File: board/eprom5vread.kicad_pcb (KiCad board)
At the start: 4 copper layers, 161 x 112 mm, 59 parts, among them J101 DEBUG, J102 UART, J201 Conn_02x21_Counter_Clockwise, J301 Barrel_Jack, SW101 RST, U101 STM32G0B0CETx, U201 TXB0108PW, U202 TXB0108PW, U203 TXB0108PW, U204 TXB0108PW, U205 TXB0108PW, U301 NCP1117ST33T3G, U302 NCP1117ST50T3G

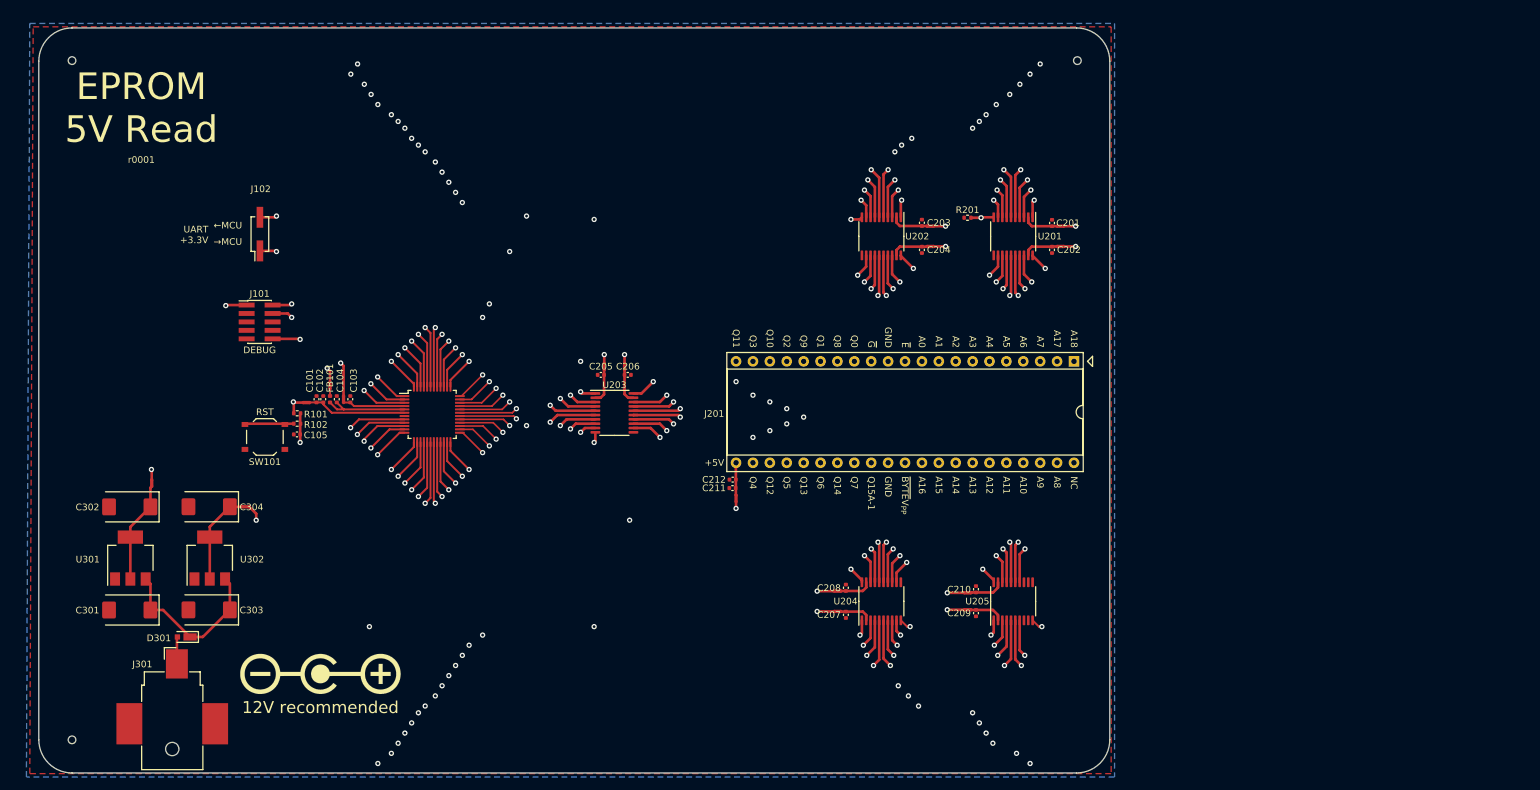
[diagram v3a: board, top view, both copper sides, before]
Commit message: redo board to use I2C port expanders (and smaller MCU)
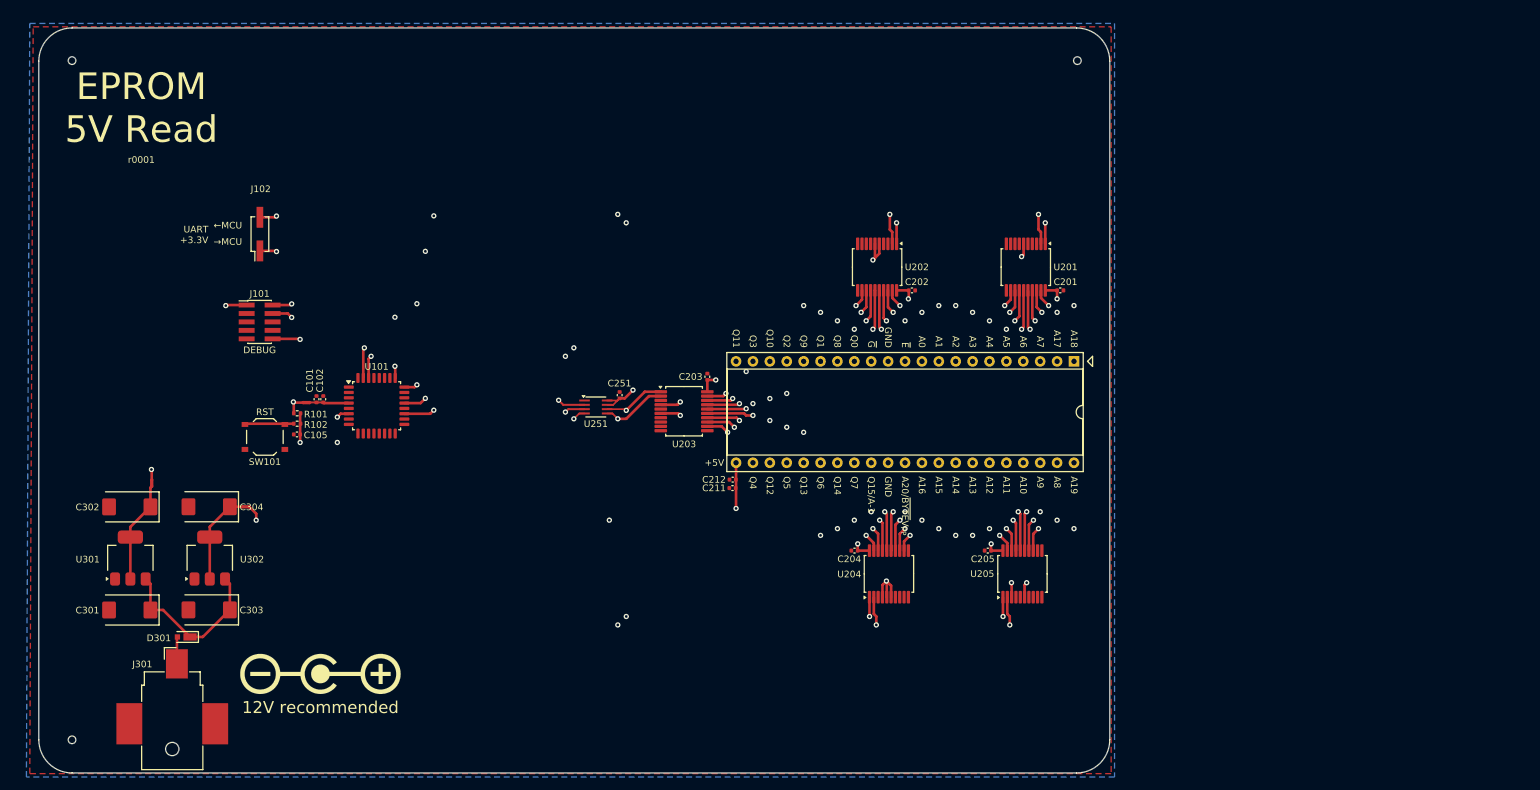
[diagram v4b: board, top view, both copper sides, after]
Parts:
- removed C103: 1µF, Capacitor_SMD:C_0402_1005Metric
- removed C104, C206, C207, C208, C209, C210: 100nF, Capacitor_SMD:C_0402_1005Metric
- removed FB101: 600Ω @ 100MHz, Inductor_SMD:L_0402_1005Metric
- removed NT102, NT103, NT14, NT201, NT202, NT203, NT204, NT205, NT206, NT207, NT208, NT209, NT210: NetTie_2, NetTie:NetTie-2_SMD_Pad0.5mm
- removed R201: 10kΩ, Resistor_SMD:R_0402_1005Metric
- added C251: 100nF, Capacitor_SMD:C_0402_1005Metric, F.Cu at (131.9, 82.3)
- added U251: PCA9306DCTR, Package_SO:SSOP-8_2.95x2.8mm_P0.65mm, F.Cu at (128.3, 84.1)
- U101: footprint Package_QFP:LQFP-48_7x7mm_P0.5mm -> Package_QFP:LQFP-32_7x7mm_P0.8mm
- U201, U202, U203, U204, U205: value TXB0108PW -> MCP23008-E/SS; footprint Package_SO:TSSOP-20_4.4x6.5mm_P0.65mm -> Package_SO:SSOP-20_5.3x7.2mm_P0.65mm
- moved C205 63.9 mm to (187.2, 105.7), turned to 0 degrees
- moved C204 46.3 mm to (167.2, 105.7), turned to 0 degrees
- moved C203 39.7 mm to (145.0, 79.5), turned to -90 degrees
- moved C202 21.9 mm to (175.8, 66.5), turned to 180 degrees
- moved U203 10.5 mm to (141.5, 84.7)
- moved C201 10.2 mm to (198.1, 66.5), turned to 180 degrees
- moved U101 8.45 mm to (95.3, 83.9)
- moved U201 5.00 mm to (192.9, 63.0)
- moved U202 4.67 mm to (170.6, 63.0)
- moved U205 4.35 mm to (192.4, 109.2)
- moved U204 4.27 mm to (172.3, 109.2)
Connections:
- net /EPROM/5V_A0 renamed /EPROM/A0
- net /EPROM/5V_A10 renamed /EPROM/A10
- net /EPROM/5V_A11 renamed /EPROM/A11
- net /EPROM/5V_A12 renamed /EPROM/A12
- net /EPROM/5V_A14 renamed /EPROM/A14
- net /EPROM/5V_A15 renamed /EPROM/A15
- net /EPROM/5V_A16 renamed /EPROM/A16
- net /EPROM/5V_A17 renamed /EPROM/A17
- net /EPROM/5V_A2 renamed /EPROM/A2
- net /EPROM/5V_A3 renamed /EPROM/A3
- net /EPROM/5V_A4 renamed /EPROM/A4
- net /EPROM/5V_A5 renamed /EPROM/A5
- net /EPROM/5V_A6 renamed /EPROM/A6
- net /EPROM/5V_A7 renamed /EPROM/A7
- net /EPROM/5V_A8 renamed /EPROM/A8
- net /EPROM/5V_A9 renamed /EPROM/A9
- net /EPROM/5V_Q0 renamed /EPROM/Q0
- net /EPROM/5V_Q1 renamed /EPROM/Q1
- net /EPROM/5V_Q14 renamed /EPROM/Q14
- net /EPROM/5V_Q15A-1 renamed /EPROM/Q15_A-1
- net /EPROM/5V_Q7 renamed /EPROM/Q7
- net /EPROM/5V_Q8 renamed /EPROM/Q8
- net /EPROM/5V_Q9 renamed /EPROM/Q9
- net /EPROM/5V_~{BYTE}V_{PP} renamed /EPROM/A20_~{BYTE}V_{PP}
- net /EPROM/5V_~{E} renamed /EPROM/~{E}
- net /EPROM/5V_~{G} renamed /EPROM/~{G}
- C201 pad 1: Net-(U201-V_{CCA}) -> /EPROM/GND
- C201 pad 2: /EPROM/GND -> /EPROM/+5V
- C202 pad 1: Net-(U201-V_{CCB}) -> /EPROM/GND
- C202 pad 2: /EPROM/GND -> /EPROM/+5V
- C203 pad 1: Net-(U202-V_{CCA}) -> /EPROM/GND
- C203 pad 2: /EPROM/GND -> /EPROM/+5V
- C204 pad 1: Net-(U202-V_{CCB}) -> /EPROM/GND
- C204 pad 2: /EPROM/GND -> /EPROM/+5V
- C205 pad 1: Net-(U203-V_{CCA}) -> /EPROM/GND
- C205 pad 2: /EPROM/GND -> /EPROM/+5V
- C211 pad 2: /EPROM/5V_V_{CC} -> /EPROM/+5V
- C212 pad 2: /EPROM/5V_V_{CC} -> /EPROM/+5V
- J201 pad 1: /EPROM/5V_A18 -> /EPROM/A18
- J201 pad 18: /EPROM/5V_Q2 -> /EPROM/Q2
- J201 pad 19: /EPROM/5V_Q10 -> /EPROM/Q10
- J201 pad 20: /EPROM/5V_Q3 -> /EPROM/Q3
- J201 pad 21: /EPROM/5V_Q11 -> /EPROM/Q11
- J201 pad 22: /EPROM/5V_V_{CC} -> /EPROM/+5V
- J201 pad 23: /EPROM/5V_Q4 -> /EPROM/Q4
- J201 pad 24: /EPROM/5V_Q12 -> /EPROM/Q12
- J201 pad 25: /EPROM/5V_Q5 -> /EPROM/Q5
- J201 pad 26: /EPROM/5V_Q13 -> /EPROM/Q13
- J201 pad 27: /EPROM/5V_Q6 -> /EPROM/Q6
- J201 pad 36: /EPROM/5V_A13 -> /EPROM/A13
- J201 pad 42: /EPROM/NC -> /EPROM/A19
- J201 pad 9: /EPROM/5V_A1 -> /EPROM/A1
- U101 pad 1: /A5 -> unconnected-(U101-PB9-Pad1)
- U101 pad 10: /MCU/MCU Debug/~{RST} -> unconnected-(U101-PA3-Pad10)
- U101 pad 11: /LSOE -> unconnected-(U101-PA4-Pad11)
- U101 pad 12: /A8 -> unconnected-(U101-PA5-Pad12)
- U101 pad 13: /A9 -> unconnected-(U101-PA6-Pad13)
- U101 pad 14: /A10 -> unconnected-(U101-PA7-Pad14)
- U101 pad 15: /A11 -> unconnected-(U101-PB0-Pad15)
- U101 pad 16: /A12 -> unconnected-(U101-PB1-Pad16)
- U101 pad 17: /A13 -> unconnected-(U101-PB2-Pad17)
- U101 pad 18: /A14 -> unconnected-(U101-PA8-Pad18)
- U101 pad 19: /A15 -> /MCU/UART_MCUTX
- U101 pad 2: /A6 -> unconnected-(U101-PC14-Pad2)
- U101 pad 20: /A16 -> unconnected-(U101-PC6-Pad20)
- U101 pad 21: /~{BYTE}V_{PP} -> /MCU/UART_MCURX
- U101 pad 22: /Q15A-1 -> unconnected-(U101-PA11/PA9-Pad22)
- U101 pad 23: /Q7 -> unconnected-(U101-PA12/PA10-Pad23)
- U101 pad 24: /Q14 -> /MCU/SWDIO
- U101 pad 25: /Q6 -> /MCU/SWCLK
- U101 pad 26: /Q4 -> unconnected-(U101-PA15-Pad26)
- U101 pad 27: /Q12 -> unconnected-(U101-PB3-Pad27)
- U101 pad 28: /Q5 -> unconnected-(U101-PB4-Pad28)
- U101 pad 29: /MCU/UART_MCUTX -> unconnected-(U101-PB5-Pad29)
- U101 pad 3: /A7 -> unconnected-(U101-PC15-Pad3)
- U101 pad 30: /Q13 -> /EPROM/SCL_3.3V
- U101 pad 31: /Q2 -> /EPROM/SDA_3.3V
- U101 pad 32: /MCU/UART_MCURX -> unconnected-(U101-PB8-Pad32)
- U101 pad 4: /MCU/VBAT -> /MCU/VDD
- U101 pad 5: /MCU/VREF+ -> /EPROM/GND
- U101 pad 6: /MCU/VDD -> /MCU/MCU Debug/~{RST}
- U101 pad 7: /EPROM/GND -> unconnected-(U101-PA0-Pad7)
- U101 pad 8: /A17 -> unconnected-(U101-PA1-Pad8)
- U101 pad 9: /A18 -> unconnected-(U101-PA2-Pad9)
- U201 pad 1: /A18 -> /EPROM/SCL
- U201 pad 10: /LSOE -> unconnected-(U201-NC-Pad10)
- U201 pad 11: /EPROM/GND -> unconnected-(U201-NC-Pad11)
- U201 pad 19: Net-(U201-V_{CCB}) -> /EPROM/A18
- U201 pad 2: Net-(U201-V_{CCA}) -> /EPROM/SDA
- U201 pad 20: /EPROM/5V_A18 -> /EPROM/+5V
- U201 pad 3: /A17 -> /EPROM/GND
- U201 pad 4: /A7 -> /EPROM/GND
- U201 pad 5: /A6 -> /EPROM/GND
- U201 pad 6: /A5 -> /EPROM/+5V
- U201 pad 7: /A4 -> unconnected-(U201-NC-Pad7)
- U201 pad 8: /A3 -> unconnected-(U201-INT-Pad8)
- U201 pad 9: /A2 -> /EPROM/GND
- U202 pad 1: /A1 -> /EPROM/SCL
- U202 pad 10: /LSOE -> unconnected-(U202-NC-Pad10)
- U202 pad 11: /EPROM/GND -> unconnected-(U202-NC-Pad11)
- U202 pad 19: Net-(U202-V_{CCB}) -> /EPROM/A1
- U202 pad 2: Net-(U202-V_{CCA}) -> /EPROM/SDA
- U202 pad 20: /EPROM/5V_A1 -> /EPROM/+5V
- U202 pad 3: /A0 -> /EPROM/GND
- U202 pad 4: /ROM_~{CS} -> /EPROM/GND
- U202 pad 5: /ROM_~{OE} -> /EPROM/+5V
- U202 pad 6: /Q0 -> /EPROM/+5V
- U202 pad 7: /Q8 -> unconnected-(U202-NC-Pad7)
- U202 pad 8: /Q1 -> unconnected-(U202-INT-Pad8)
- U202 pad 9: /Q9 -> /EPROM/GND
- U203 pad 1: /Q11 -> /EPROM/SCL
- U203 pad 10: /LSOE -> unconnected-(U203-NC-Pad10)
- U203 pad 11: /EPROM/GND -> unconnected-(U203-NC-Pad11)
- U203 pad 12: /EPROM/5V_Q4 -> /EPROM/Q13
- U203 pad 13: /EPROM/5V_Q12 -> /EPROM/Q5
- U203 pad 14: /EPROM/5V_Q5 -> /EPROM/Q12
- U203 pad 15: /EPROM/5V_Q13 -> /EPROM/Q4
- U203 pad 16: /EPROM/5V_Q2 -> /EPROM/Q11
- U203 pad 17: /EPROM/5V_Q10 -> /EPROM/Q3
- U203 pad 18: /EPROM/5V_Q3 -> /EPROM/Q10
- U203 pad 19: Net-(U203-V_{CCB}) -> /EPROM/Q2
- U203 pad 2: Net-(U203-V_{CCA}) -> /EPROM/SDA
- U203 pad 20: /EPROM/5V_Q11 -> /EPROM/+5V
- U203 pad 3: /Q3 -> /EPROM/GND
- U203 pad 4: /Q10 -> /EPROM/+5V
- U203 pad 5: /Q2 -> /EPROM/GND
- U203 pad 6: /Q13 -> /EPROM/+5V
- U203 pad 7: /Q5 -> unconnected-(U203-NC-Pad7)
- U203 pad 8: /Q12 -> unconnected-(U203-INT-Pad8)
- U203 pad 9: /Q4 -> /EPROM/GND
- U204 pad 1: /Q6 -> /EPROM/SCL
- U204 pad 10: /LSOE -> unconnected-(U204-NC-Pad10)
- U204 pad 11: /EPROM/GND -> unconnected-(U204-NC-Pad11)
- U204 pad 19: Net-(U204-V_{CCB}) -> /EPROM/Q6
- U204 pad 2: Net-(U204-V_{CCA}) -> /EPROM/SDA
- U204 pad 20: /EPROM/5V_Q6 -> /EPROM/+5V
- U204 pad 3: /Q14 -> /EPROM/GND
- U204 pad 4: /Q7 -> /EPROM/+5V
- U204 pad 5: /Q15A-1 -> /EPROM/+5V
- U204 pad 6: /~{BYTE}V_{PP} -> /EPROM/+5V
- U204 pad 7: /A16 -> unconnected-(U204-NC-Pad7)
- U204 pad 8: /A15 -> unconnected-(U204-INT-Pad8)
- U204 pad 9: /A14 -> /EPROM/GND
- U205 pad 1: /A13 -> /EPROM/SCL
- U205 pad 10: /LSOE -> unconnected-(U205-NC-Pad10)
- U205 pad 11: /EPROM/GND -> unconnected-(U205-NC-Pad11)
- U205 pad 13: unconnected-(U205-B7-Pad13) -> /EPROM/A19
- U205 pad 19: Net-(U205-V_{CCB}) -> /EPROM/A13
- U205 pad 2: Net-(U205-V_{CCA}) -> /EPROM/SDA
- U205 pad 20: /EPROM/5V_A13 -> /EPROM/+5V
- U205 pad 3: /A12 -> /EPROM/+5V
- U205 pad 4: /A11 -> /EPROM/GND
- U205 pad 5: /A10 -> /EPROM/GND
- U205 pad 6: /A9 -> /EPROM/+5V
- U205 pad 7: /A8 -> unconnected-(U205-NC-Pad7)
- U205 pad 9: unconnected-(U205-A8-Pad9) -> /EPROM/GND
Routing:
- net /LSOE: track 264.1 -> 0.00 mm, vias 9 -> 0
- net /EPROM/SDA: track 0.00 -> 211.8 mm, vias 0 -> 7
- net /EPROM/SCL: track 0.00 -> 199.8 mm, vias 0 -> 7
- net /A18: track 189.6 -> 0.00 mm, vias 4 -> 0
- net /A17: track 186.1 -> 0.00 mm, vias 4 -> 0
- net /A7: track 172.4 -> 0.00 mm, vias 4 -> 0
- net /A8: track 172.1 -> 0.00 mm, vias 4 -> 0
- net /A6: track 165.0 -> 0.00 mm, vias 4 -> 0
- net /A9: track 162.9 -> 0.00 mm, vias 4 -> 0
- net /A5: track 157.0 -> 0.00 mm, vias 4 -> 0
- net /A10: track 155.5 -> 0.00 mm, vias 4 -> 0
- net /A11: track 150.3 -> 0.00 mm, vias 4 -> 0
- net /A4: track 148.4 -> 0.00 mm, vias 4 -> 0
- net /A12: track 145.2 -> 0.00 mm, vias 4 -> 0
- net /A3: track 144.3 -> 0.00 mm, vias 4 -> 0
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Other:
- board text added: "A19"
- board text added: "A20/~{BYTE}V_{PP}"
- board text added: "Q15/A-1"
- board text removed: "NC"
- board text removed: "Q15A-1"
- board text removed: "~{BYTE}V_{PP}"

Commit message: allow driving ~RESET pins of I2C I/O expanders, add missing resistors
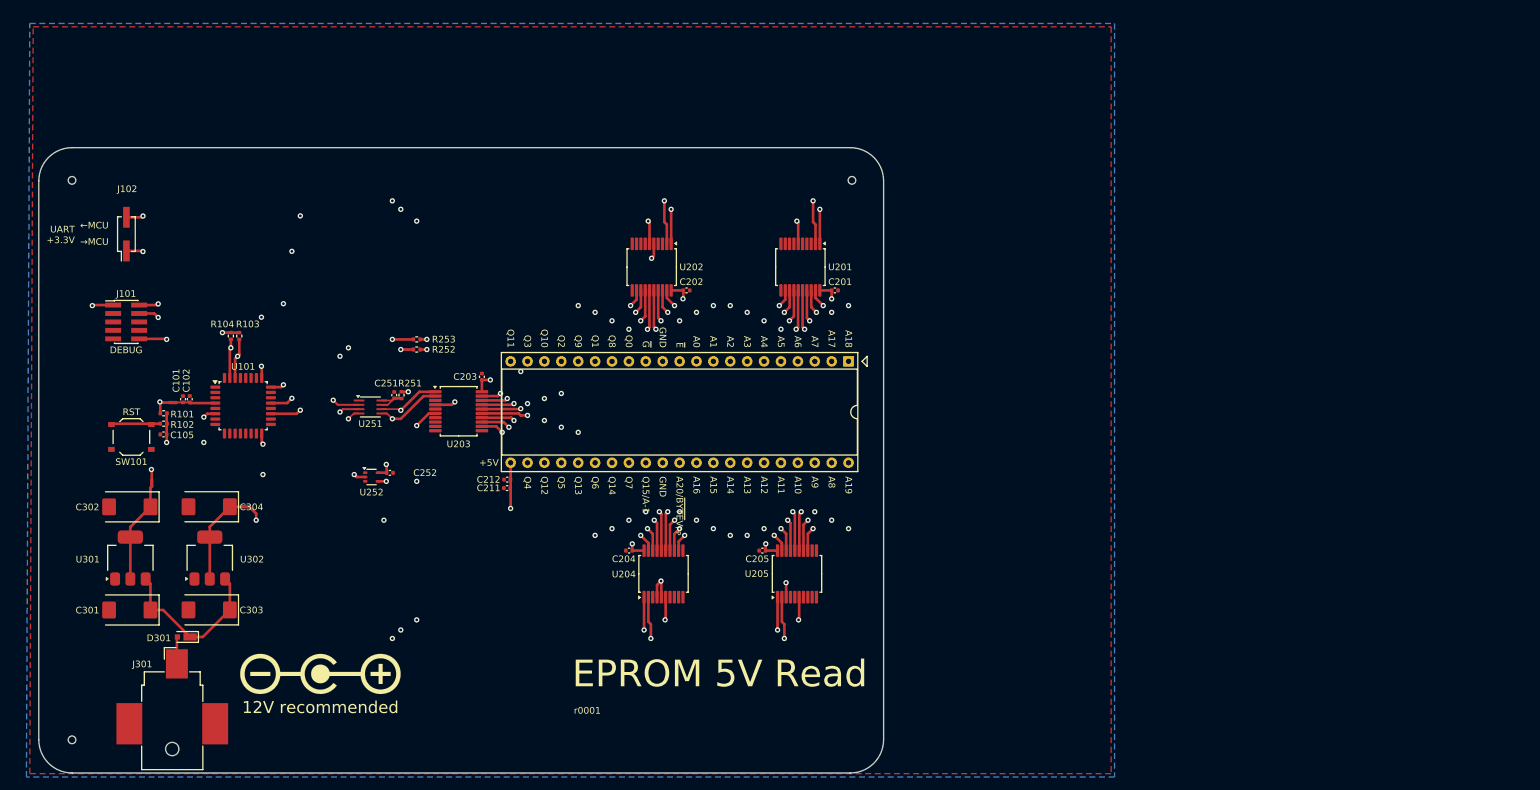
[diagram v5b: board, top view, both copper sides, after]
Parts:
- added C252: 100nF, Capacitor_SMD:C_0402_1005Metric, F.Cu at (97.3, 94.0)
- added R103: 10kΩ, Resistor_SMD:R_0402_1005Metric, F.Cu at (74.7, 73.4)
- added R104: 10kΩ, Resistor_SMD:R_0402_1005Metric, F.Cu at (73.4, 73.4)
- added R251: 200kΩ, Resistor_SMD:R_0402_1005Metric, F.Cu at (99.1, 82.3)
- added R252: 10kΩ, Resistor_SMD:R_0402_1005Metric, F.Cu at (101.3, 75.4)
- added R253: 10kΩ, Resistor_SMD:R_0402_1005Metric, F.Cu at (101.3, 73.9)
- added U252: SN74LV1T34DCK, Package_TO_SOT_SMD:SOT-353_SC-70-5, F.Cu at (94.6, 94.6)
- moved REF2 38.4 mm to (166.8, 50.0)
- moved C201 33.9 mm to (164.2, 66.5)
- moved C205 33.9 mm to (153.3, 105.7)
- moved C251 33.9 mm to (98.0, 82.3)
- moved U204 33.9 mm to (138.4, 109.2)
- moved U205 33.9 mm to (158.5, 109.2)
- moved U251 33.9 mm to (94.4, 84.1)
- moved C211 33.9 mm to (114.9, 96.3)
- moved C202 33.9 mm to (141.9, 66.5)
- moved C203 33.9 mm to (111.1, 79.5)
- moved C204 33.9 mm to (133.3, 105.7)
- moved C212 33.9 mm to (115.0, 95.0)
- moved J201 33.9 mm to (166.3, 77.2)
- moved U201 33.9 mm to (159.0, 63.0)
- moved U202 33.9 mm to (136.7, 63.0)
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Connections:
- C251 pad 2: /EPROM/+5V -> Net-(U251-EN)
- U101 pad 16: unconnected-(U101-PB1-Pad16) -> /EPROM/~{RESET}_3.3V
- U201 pad 6: /EPROM/+5V -> /EPROM/~{RESET}
- U202 pad 6: /EPROM/+5V -> /EPROM/~{RESET}
- U203 pad 6: /EPROM/+5V -> /EPROM/~{RESET}
- U204 pad 6: /EPROM/+5V -> /EPROM/~{RESET}
- U205 pad 6: /EPROM/+5V -> /EPROM/~{RESET}
- U251 pad 7: /EPROM/+5V -> Net-(U251-EN)
- U251 pad 8: /EPROM/+5V -> Net-(U251-EN)
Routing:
- net /EPROM/~{RESET}: track 0.00 -> 197.8 mm, vias 0 -> 9
- net /EPROM/+5V: track 110.1 -> 61.8 mm
- net /EPROM/~{RESET}_3.3V: track 0.00 -> 21.8 mm, vias 0 -> 3
- net /EPROM/SDA: track 211.8 -> 227.1 mm, vias 7 -> 8
- net /EPROM/SCL: track 199.8 -> 214.4 mm, vias 7 -> 8
- net /EPROM/SDA_3.3V: track 48.4 -> 36.1 mm
- net /EPROM/SCL_3.3V: track 44.1 -> 32.9 mm
- net Net-(U251-EN): track 0.00 -> 5.37 mm
- net /EPROM/+3.3V: track 12.1 -> 14.7 mm, vias 4 -> 5
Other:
- board size 161 x 112 mm -> 127 x 94 mm
